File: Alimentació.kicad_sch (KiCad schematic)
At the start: 48 parts, among them J1 USB_C_Receptacle_PowerOnly_6P, J14 Conn_01x02_Pin, J7 XT-30 male, Q1 QM6015D, U2 BQ25628ERYKR, U3 TPS611781RNWR, U4 TLV61070ADBV

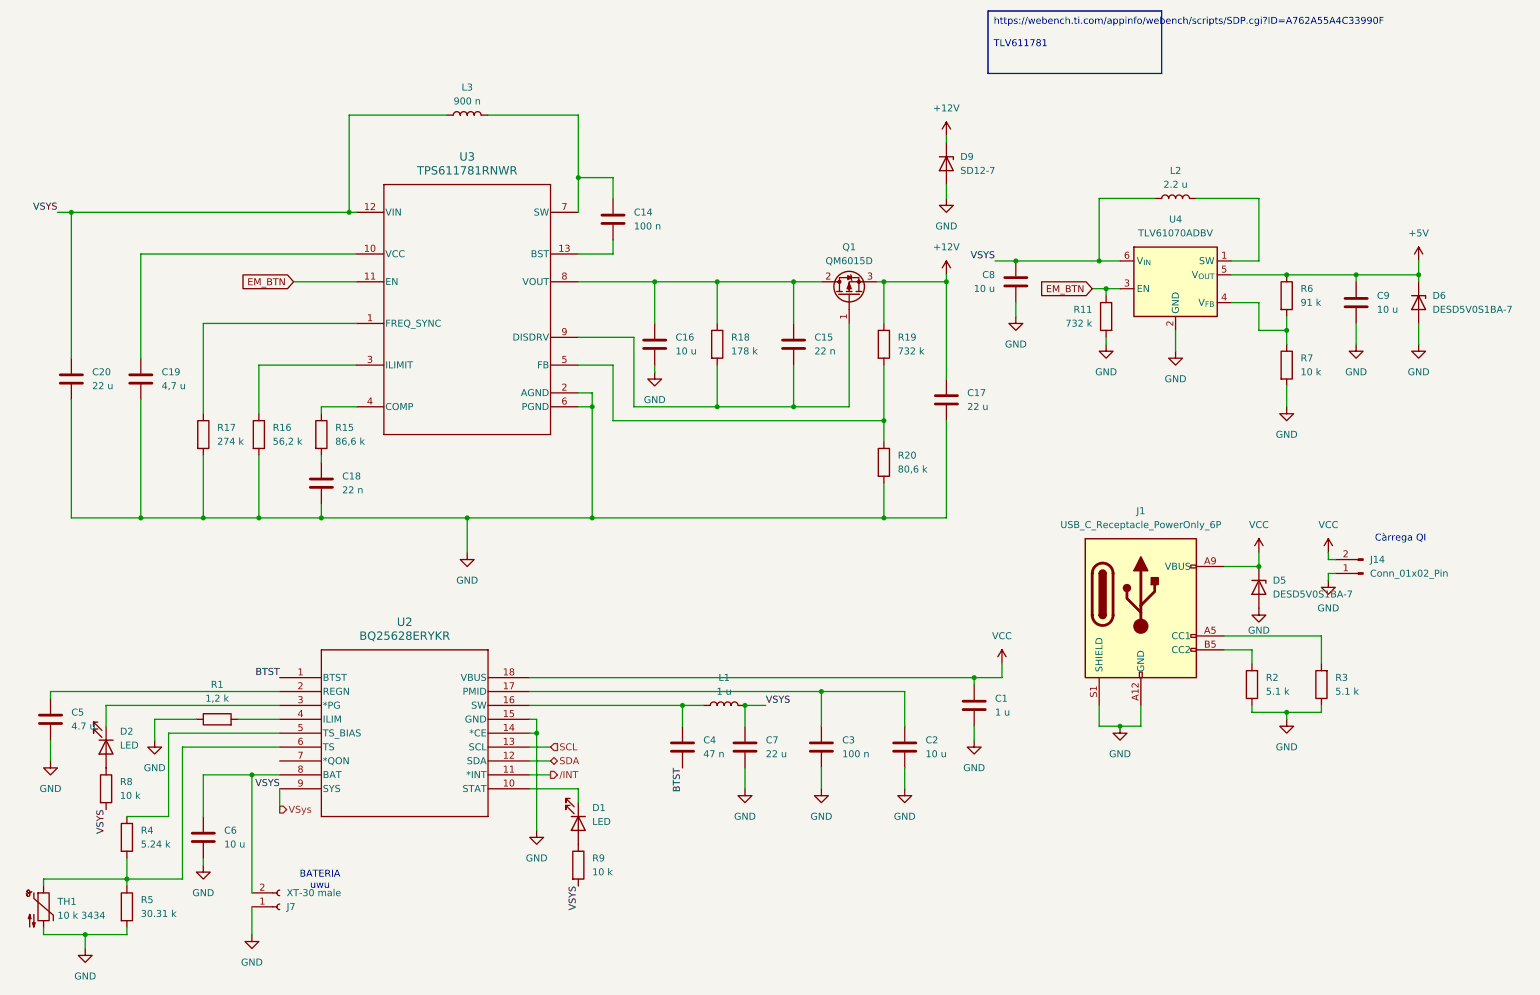
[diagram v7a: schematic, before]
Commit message: Nou esquemàtic
Nou esquemàtic per bateria en sèrie de dues cèl·les, boost de 12 V extern, i buck de 5 V.
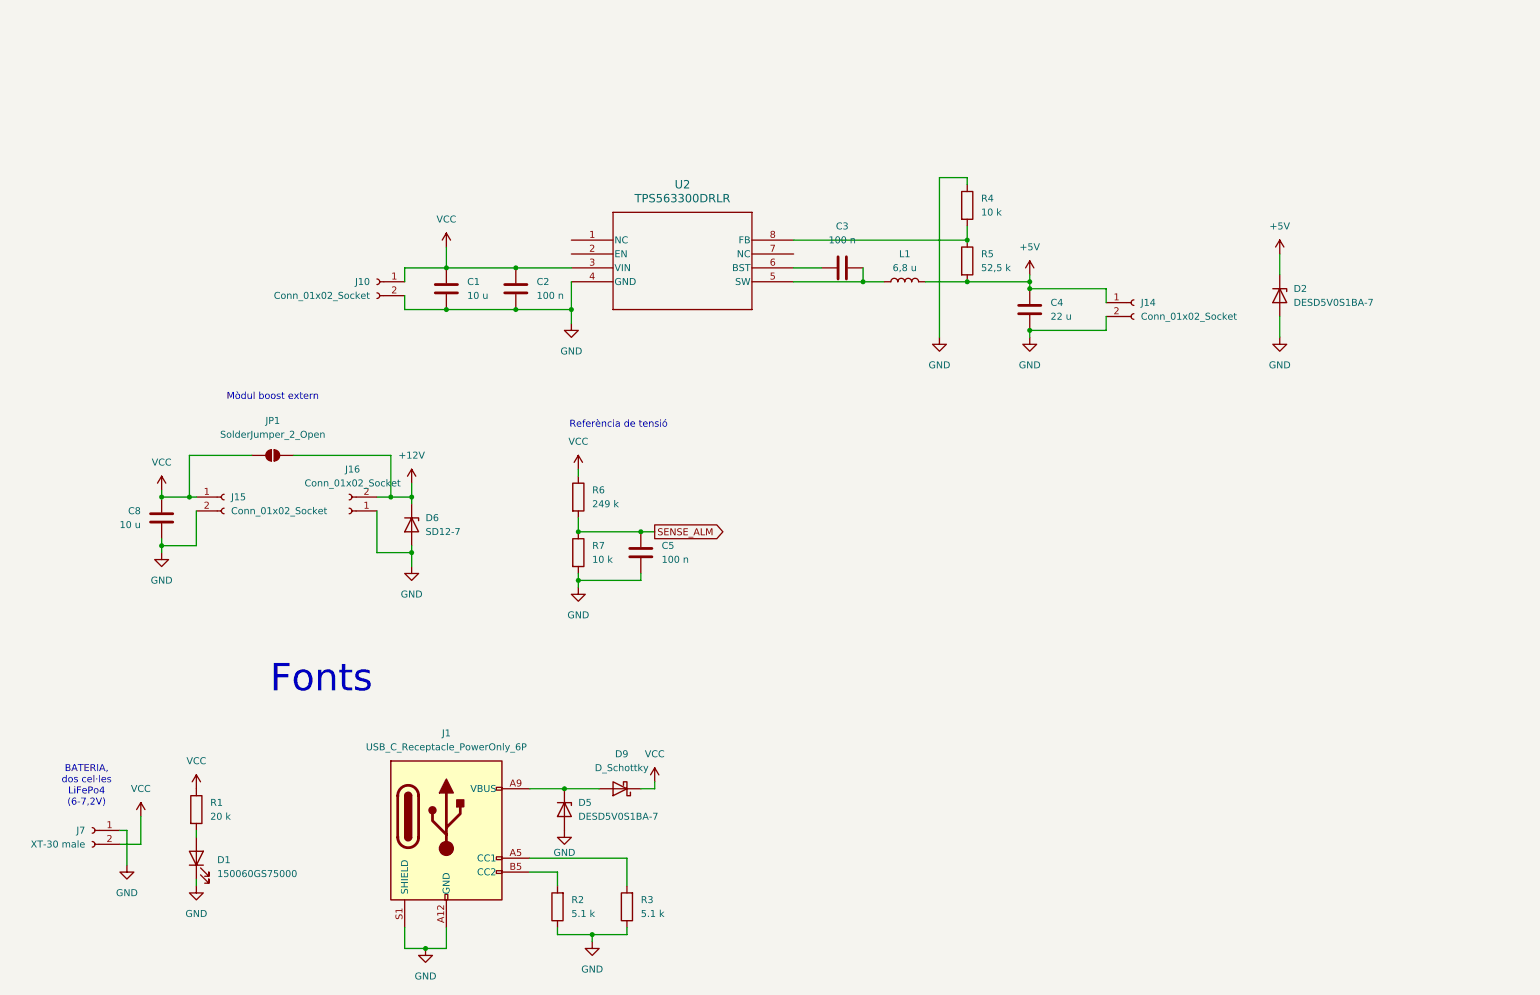
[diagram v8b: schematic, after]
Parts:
- removed C14: 100 n, Capacitor_SMD:C_0603_1608Metric_Pad1.08x0.95mm_HandSolder, symbol Device:C
- removed C15, C18: 22 n, Capacitor_SMD:C_0603_1608Metric_Pad1.08x0.95mm_HandSolder, symbol Device:C
- removed C16, C6, C9: 10 u, Capacitor_SMD:C_0603_1608Metric_Pad1.08x0.95mm_HandSolder, symbol Device:C
- removed C17, C20, C7: 22 u, Capacitor_SMD:C_0603_1608Metric_Pad1.08x0.95mm_HandSolder, symbol Device:C
- removed C19: 4,7 u, Capacitor_SMD:C_0603_1608Metric_Pad1.08x0.95mm_HandSolder, symbol Device:C
- removed D2: LED, Diode_SMD:D_0603_1608Metric, symbol Device:LED
- removed D9: SD12-7, Diode_SMD:D_SOD-323, symbol Device:D_Zener
- removed J14: Conn_01x02_Pin, Connector_JST:JST_PH_B2B-PH-K_1x02_P2.00mm_Vertical, symbol Connector:Conn_01x02_Pin
- removed L2: 2.2 u, Inductor_SMD:L_1008_2520Metric_Pad1.43x2.20mm_HandSolder, symbol Device:L
- removed L3: 900 n, Inductor_SMD:L_1008_2520Metric_Pad1.43x2.20mm_HandSolder, symbol Device:L
- removed Q1: QM6015D, Package_TO_SOT_SMD:TO-252-2, symbol Transistor_FET:QM6015D
- removed R11, R19: 732 k, Resistor_SMD:R_0603_1608Metric, symbol Device:R
- removed R15: 86,6 k, Resistor_SMD:R_0603_1608Metric, symbol Device:R
- removed R16: 56,2 k, Resistor_SMD:R_0603_1608Metric, symbol Device:R
- removed R17: 274 k, Resistor_SMD:R_0603_1608Metric, symbol Device:R
- removed R18: 178 k, Resistor_SMD:R_0603_1608Metric, symbol Device:R
- removed R20: 80,6 k, Resistor_SMD:R_0603_1608Metric, symbol Device:R
- removed R8, R9: 10 k, Resistor_SMD:R_0603_1608Metric, symbol Device:R
- removed TH1: 10 k 3434, Resistor_SMD:R_0603_1608Metric_Pad0.98x0.95mm_HandSolder, symbol Device:Thermistor_NTC
- removed U2: BQ25628ERYKR, BQ25628E:WQFN-HR18__RYK_TEX, symbol BQ25628E:BQ25628ERYKR
- removed U3: TPS611781RNWR, tps611781rnwr:RNW0013A, symbol TPS61178:TPS611781RNWR
- removed U4: TLV61070ADBV, Package_TO_SOT_SMD:SOT-23-6, symbol Regulator_Switching:TLV61070ADBV
- added D2: DESD5V0S1BA-7, Diode_SMD:D_SOD-323, symbol Device:D_Zener
- added D9: D_Schottky, Diode_SMD:D_SOD-323, symbol Device:D_Schottky
- added J10, J14, J15, J16: Conn_01x02_Socket, Connector_PinSocket_2.54mm:PinSocket_1x02_P2.54mm_Vertical, symbol Connector:Conn_01x02_Socket
- added JP1: SolderJumper_2_Open, Jumper:SolderJumper-2_P1.3mm_Open_RoundedPad1.0x1.5mm, symbol Jumper:SolderJumper_2_Open
- added U2: TPS563300DRLR, SOT5X3-8_DRL_TEX, symbol TPS563300:TPS563300DRLR
- C1: value 1 u -> 10 u
- C2: value 10 u -> 100 n
- C4: value 47 n -> 22 u
- C5: value 4.7 u -> 100 n
- D1: value LED -> 150060GS75000; footprint Diode_SMD:D_0603_1608Metric -> LED_SMD:LED_0603_1608Metric_Pad1.05x0.95mm_HandSolder
- D6: value DESD5V0S1BA-7 -> SD12-7
- L1: value 1 u -> 6,8 u; footprint Inductor_SMD:L_1008_2520Metric_Pad1.43x2.20mm_HandSolder -> HM72L-06306R8LFTR:INDPM7166X300N
- R1: value 1,2 k -> 20 k; footprint Resistor_SMD:R_0603_1608Metric -> Resistor_SMD:R_0603_1608Metric_Pad0.98x0.95mm_HandSolder
- R4: value 5.24 k -> 10 k; footprint Resistor_SMD:R_0603_1608Metric -> Resistor_SMD:R_0603_1608Metric_Pad0.98x0.95mm_HandSolder
- R5: value 30.31 k -> 52,5 k; footprint Resistor_SMD:R_0603_1608Metric -> Resistor_SMD:R_0603_1608Metric_Pad0.98x0.95mm_HandSolder
- R6: value 91 k -> 249 k; footprint Resistor_SMD:R_0603_1608Metric -> Resistor_SMD:R_0603_1608Metric_Pad0.98x0.95mm_HandSolder
- R7: footprint Resistor_SMD:R_0603_1608Metric -> Resistor_SMD:R_0603_1608Metric_Pad0.98x0.95mm_HandSolder
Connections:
- net BTST is gone; now on net GND: C4.2
- net +12V: now also D6.1 (K), J16.2 (Pin_2), JP1.2 (B)
- net +5V: now also C4.1, L1.2, R5.2, D2.1 (K), J14.1 (Pin_1); no longer D6.1 (K), R6.1
- net GND: now also C1.2, D1.1 (K), R4.1, D2.2 (A), J10.2 (Pin_2), J14.2 (Pin_2), J15.2 (Pin_2), J16.1 (Pin_1), U2.4 (GND); no longer C1.1, C3.2, R1.1, R5.2
- net VCC: now also C1.1, C2.1, C8.1, J7.2 (Pin_2), R1.1, R6.1, D9.1 (K), J10.1 (Pin_1), J15.1 (Pin_1), JP1.1 (A), U2.3 (VIN); no longer C1.2, D5.1 (K), J1.A9 (VBUS), J1.B9 (VBUS)
- net SENSE_ALM: now reaches R6.2, R7.1
- net SENSE_ALM: now also C5.1
- net at C3.1: now also U2.6 (BST); no longer C2.1
- net at R1.2: now also D1.2 (A)
- net at L1.1: now also C3.2, U2.5 (SW); no longer C4.1
- net at R4.2, R5.1: now also U2.8 (FB)
- removed net VSys: C8.1, L1.2
- new net: D5.1 (K), D9.2 (A), J1.A9 (VBUS), J1.B9 (VBUS)
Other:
- note added: "BATERIA, dos cel·les LiFePo4 (6-7,2V)"
- note added: "Fonts"
- note added: "Mòdul boost extern"
- note added: "Referència de tensió"
- note removed: "BATERIA uwu"
- note removed: "Càrrega QI"
- moved on the sheet: C8, D5, D6, J1, J7, R2, R3
